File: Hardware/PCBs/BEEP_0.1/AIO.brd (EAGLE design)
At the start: 110 x 110 mm, 70 parts, among them IC1 ULN2803ASOP18, IC2 ULN2803ASOP18, IC3 74HC238D, IC4 74HC238D, U2 TB6612FNG, U3 ATXMEGA64D3-AU, X1 MICROMATCH-8, X10 MICROMATCH-10, X2 MICROMATCH-8, X3 MICROMATCH-8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

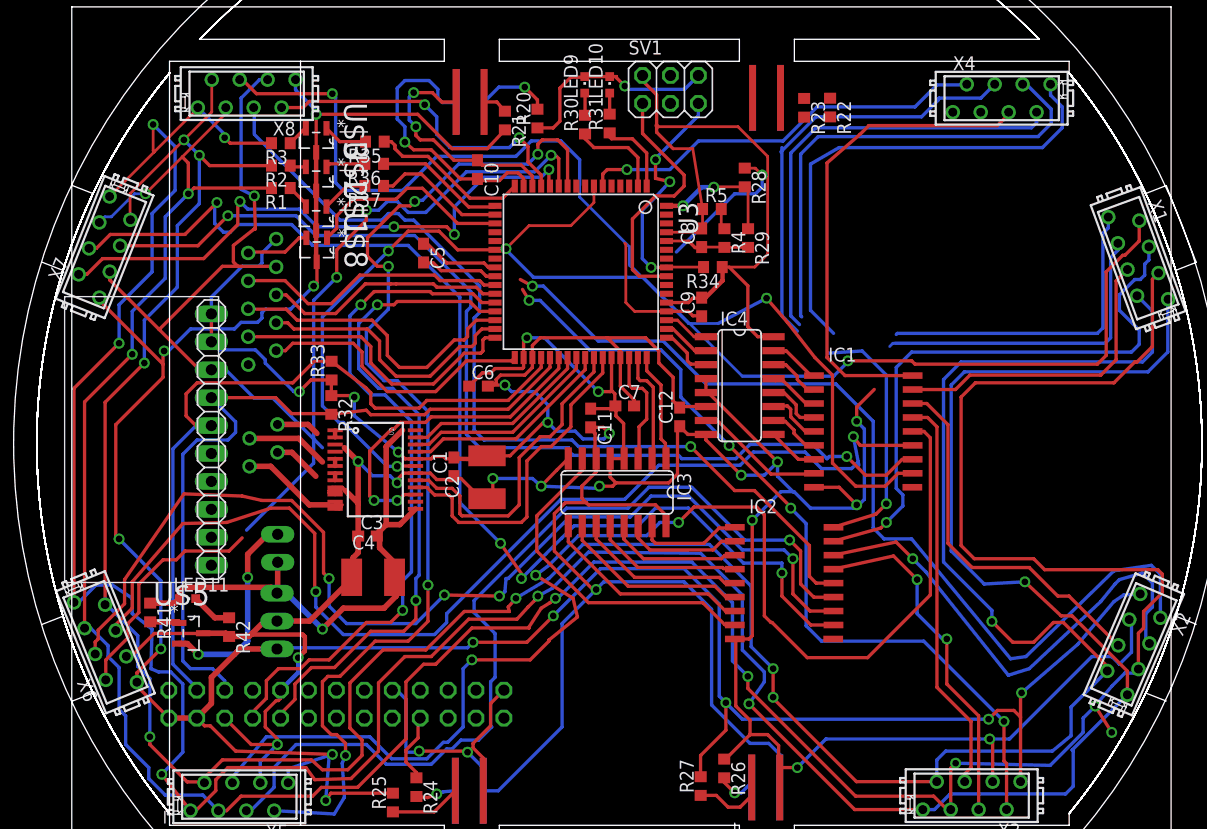
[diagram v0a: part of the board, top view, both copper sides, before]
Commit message: *add i2c connector *continue routing
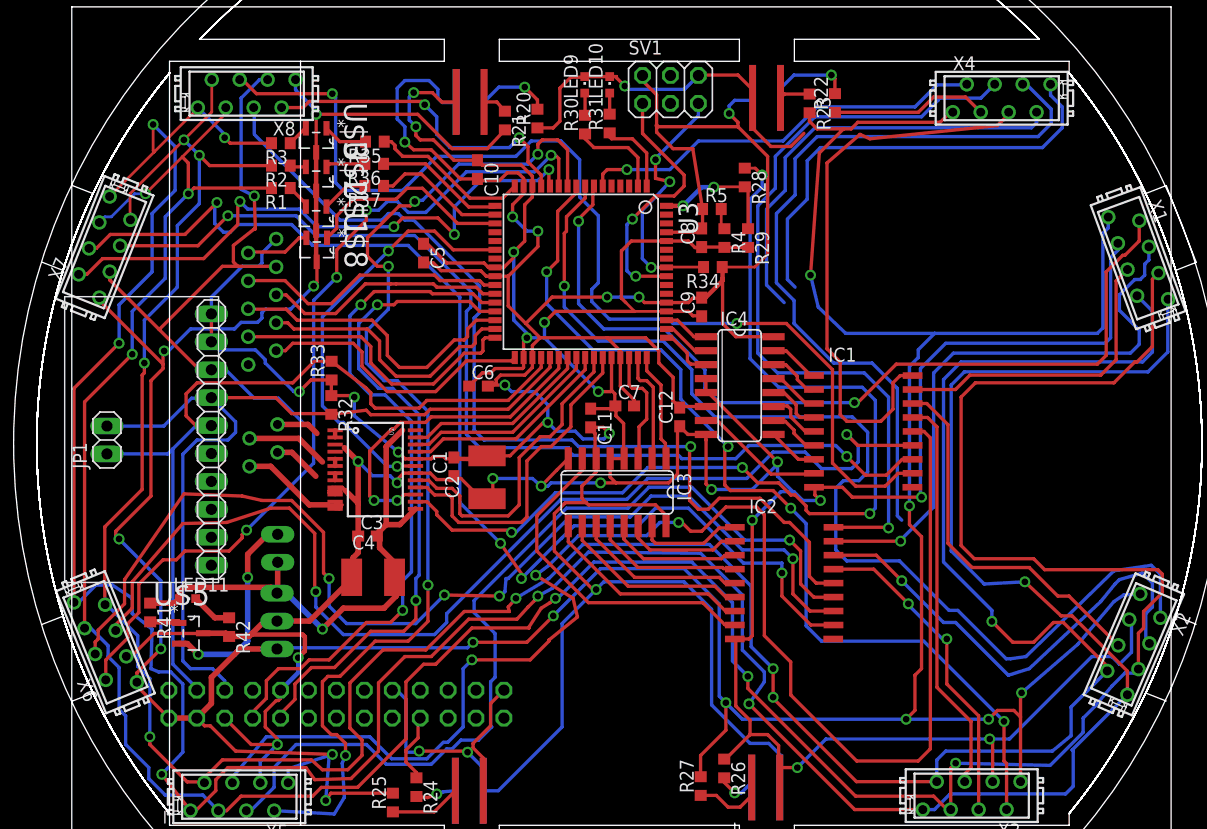
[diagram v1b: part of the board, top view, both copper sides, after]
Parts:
- added JP1: I2C, pinhead:1X02
- moved R23 0.64 mm to (67.1, 71.2)
- moved R22 0.61 mm to (69.4, 71.3), turned to 90 degrees
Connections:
- net SCL: now also JP1.2
- net SDA: now also JP1.1
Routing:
- net +5V: track 287.8 -> 364.9 mm, vias 12 -> 15
- net +7V: track 62.3 -> 138.7 mm, vias 3 -> 6
- net GND: track 451.0 -> 513.9 mm, vias 20 -> 22
- net +3V3: track 298.6 -> 336.9 mm, vias 10 -> 15
- net LED_A2_OUT: track 327.8 -> 351.2 mm, vias 8 -> 6
- net LED_K4_OUT: track 116.5 -> 136.0 mm
- net ADISTANCE_2: track 86.2 -> 99.3 mm
- net ADISTANCE_3: track 75.4 -> 86.8 mm
- net SCL: track 68.2 -> 78.8 mm
- net IR_LED_K0_OUT: track 62.6 -> 71.8 mm
- net ENCODER_L2: track 0.00 -> 7.81 mm, vias 0 -> 1
- net LED_K0_OUT: track 44.6 -> 51.6 mm
- net SDA: track 70.0 -> 76.2 mm
- net ADISTANCE_1: track 85.4 -> 79.4 mm
- net IR_LED_K7_OUT: track 82.6 -> 86.6 mm
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
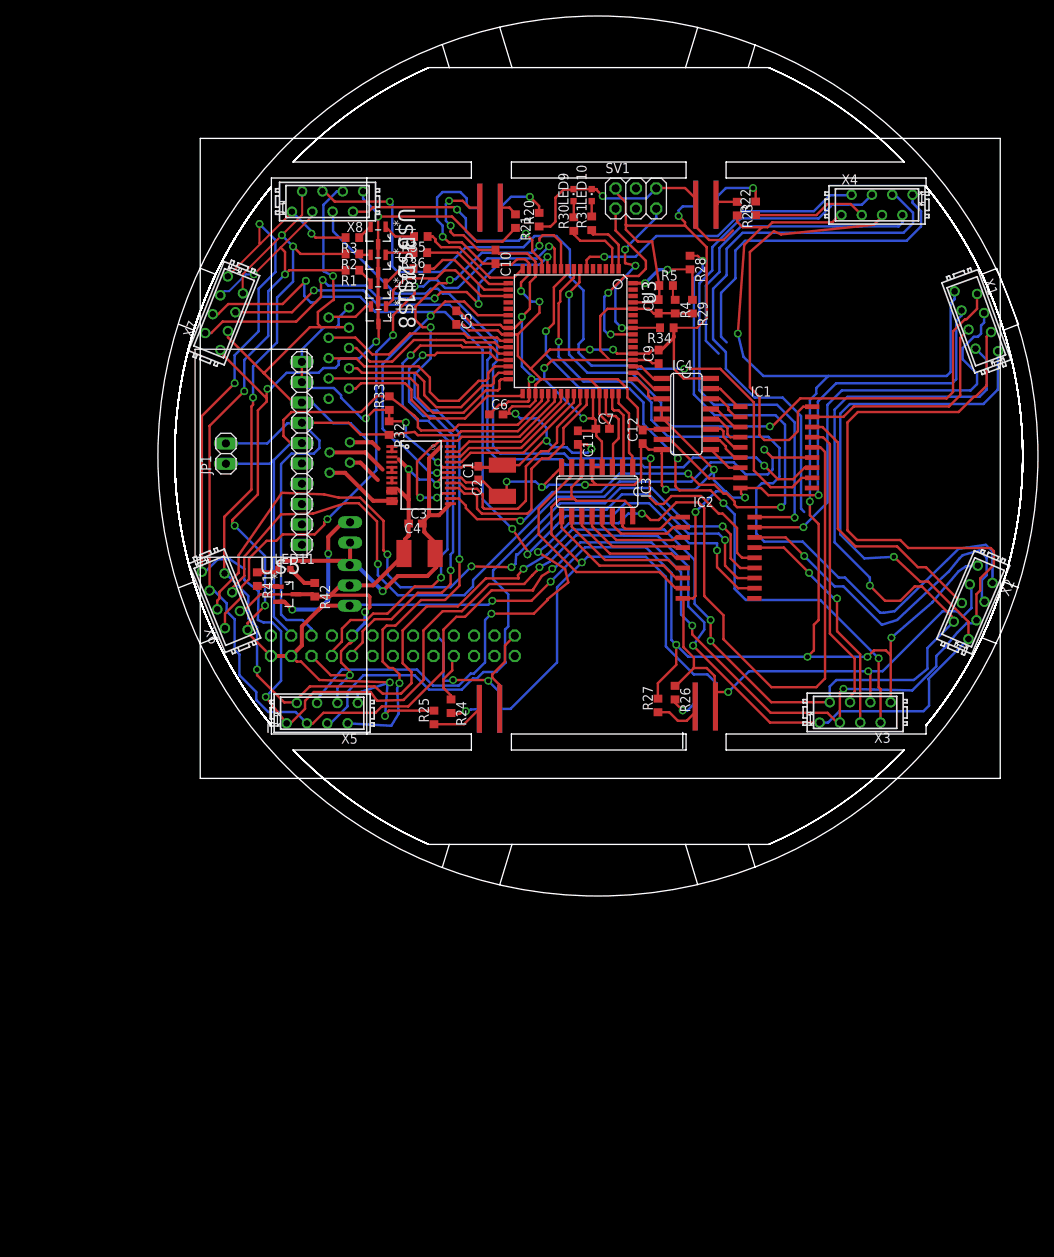
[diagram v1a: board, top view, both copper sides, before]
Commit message: add i2c header continue routing
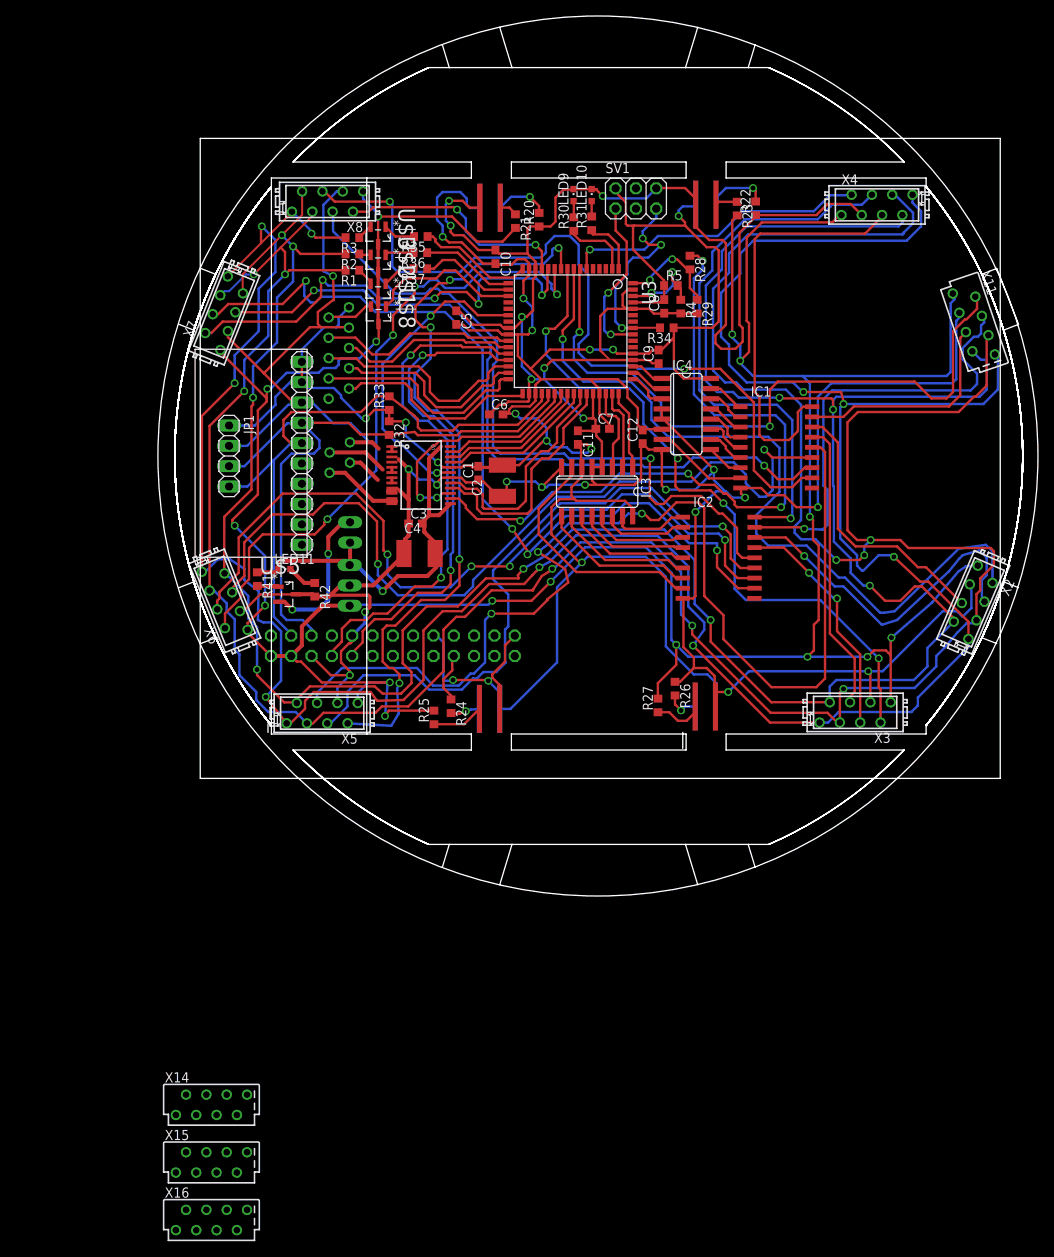
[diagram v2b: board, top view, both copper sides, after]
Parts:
- removed X1: MICROMATCH-8, Con-amp-micromatch:MICROMATCH-8
- added X11, X14, X15, X16: (no value), con-amp:FSIDE-8
- JP1: value I2C -> (none); device pinhead:1X02 -> pinhead:1X04
- moved C8 0.70 mm to (58.0, 59.0)
- moved R4 0.70 mm to (60.1, 59.0)
- moved R5 0.60 mm to (58.8, 61.6)
- moved R29 0.60 mm to (62.1, 59.0)
- moved JP1 0.50 mm to (3.60, 40.3), turned to 270 degrees
- moved R26 0.50 mm to (59.4, 11.2)
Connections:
- net +3V3: now also JP1.1
- net +5V: now also X11.1; no longer X1.8
- net ADISTANCE_1: now also X11.2; no longer X1.7
- net GND: now also JP1.2, X11.3; no longer X1.6
- net IR_LED_K1_OUT: now also X11.4; no longer X1.5
- net LED_A0_OUT: now also X11.8; no longer X1.1
- net LED_A1_OUT: now also X11.7; no longer X1.2
- net LED_A2_OUT: now also X11.6; no longer X1.3
- net LED_K1_OUT: now also X11.5; no longer X1.4
- net SCL: now also JP1.3; no longer JP1.2
- net SDA: now also JP1.4; no longer JP1.1
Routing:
- net GND: track 513.9 -> 567.9 mm
- net LED_A1_OUT: track 311.7 -> 333.7 mm, vias 8 -> 9
- net LED_A0_OUT: track 328.1 -> 349.1 mm, vias 7 -> 9
- net LED_A2_OUT: track 351.2 -> 367.4 mm, vias 6 -> 9
- net +5V: track 364.9 -> 380.9 mm, vias 15 -> 16
- net +3V3: track 336.9 -> 350.5 mm
- net N$4: track 2.08 -> 11.2 mm, vias 0 -> 2
- net LED_K5_OUT: track 99.9 -> 105.6 mm
- net ADISTANCE_1: track 79.4 -> 83.7 mm
- net PDI_DATA: track 23.7 -> 20.8 mm
- net IR_LED_K1_OUT: track 53.5 -> 56.1 mm
- net PDI_CLK: track 23.7 -> 26.1 mm
- net BATT_VOLTAGE: track 11.8 -> 14.1 mm
- net ADISTANCE_6: track 54.0 -> 56.4 mm
- net LED_K7_OUT: track 97.7 -> 99.8 mm
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
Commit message: continue routing add hardware architecture shematic
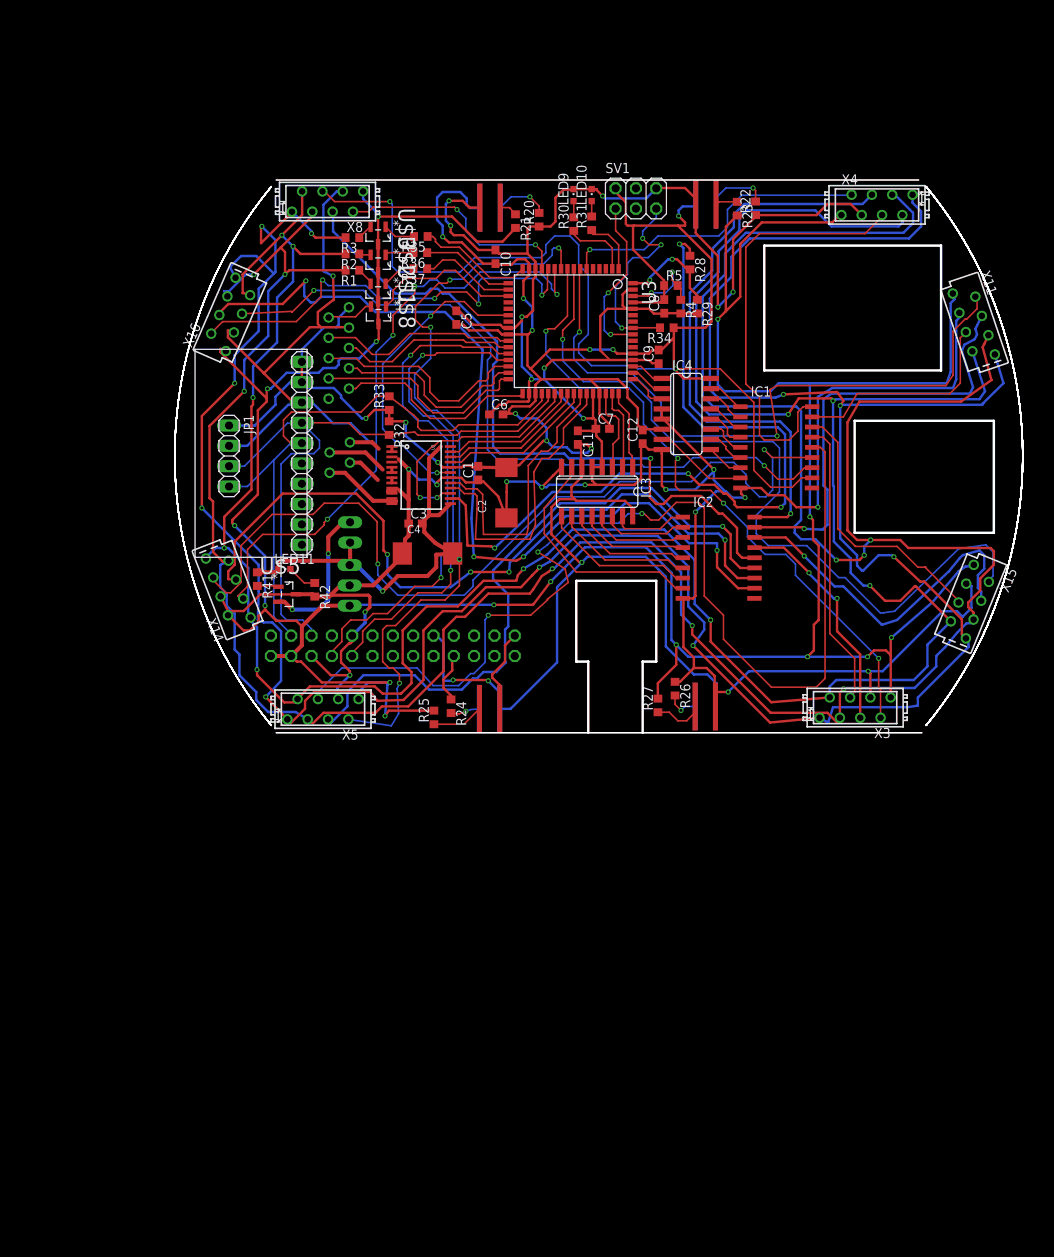
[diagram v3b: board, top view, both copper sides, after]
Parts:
- removed X2, X6, X7: MICROMATCH-8, Con-amp-micromatch:MICROMATCH-8
- C2, C4: device rcl:C1812 -> rcl:SMC_D
- moved X15 117.9 mm to (96.2, 22.1), turned to 247.9 degrees
- moved X16 113.2 mm to (3.80, 58.0), turned to 66.5 degrees
- moved X14 64.6 mm to (3.50, 23.8), turned to 111.2 degrees
- moved C2 1.58 mm to (38.3, 35.7)
- moved C4 1.00 mm to (28.4, 28.1)
- moved X3 0.60 mm to (81.9, 8.85)
- moved X5 0.51 mm to (15.3, 8.65)
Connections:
- net +3V3: now also C2.-; no longer C2.2
- net +5V: now also X14.2, X15.1, X16.1; no longer X2.8, X6.8, X7.8
- net +7V: now also C4.-; no longer C4.2
- net ADISTANCE_2: now also X15.2; no longer X2.7
- net ADISTANCE_5: now also X14.3; no longer X6.7
- net ADISTANCE_6: now also X16.2; no longer X7.7
- net GND: now also C2.+, C4.+, X14.4, X15.3, X16.3; no longer C2.1, C4.1, X2.6, X6.6, X7.6
- net IR_LED_K2_OUT: now also X15.4; no longer X2.5
- net IR_LED_K5_OUT: now also X14.5; no longer X6.5
- net IR_LED_K6_OUT: now also X16.4; no longer X7.5
- net LED_A0_OUT: now also X15.8, X16.8; no longer X2.1, X6.1, X7.1
- net LED_A1_OUT: now also X14.8, X15.7, X16.7; no longer X2.2, X6.2, X7.2
- net LED_A2_OUT: now also X14.7, X15.6, X16.6; no longer X2.3, X6.3, X7.3
- net LED_K2_OUT: now also X15.5; no longer X2.4
- net LED_K5_OUT: now also X14.6; no longer X6.4
- net LED_K6_OUT: now also X16.5; no longer X7.4
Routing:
- net +7V: track 138.7 -> 151.1 mm
- net LED_A1_OUT: track 333.7 -> 343.0 mm, vias 9 -> 10
- net MOTOR_B_IN1: track 28.9 -> 35.8 mm
- net MOTOR_B_IN2: track 30.5 -> 37.4 mm
- net LED_A2_OUT: track 367.4 -> 372.9 mm
- net IR_LED_K6_OUT: track 106.0 -> 111.1 mm
- net GND: track 567.9 -> 563.1 mm, vias 22 -> 24
- net ADISTANCE_3: track 87.2 -> 82.7 mm
- net ADISTANCE_5: track 80.6 -> 76.7 mm
- net +5V: track 380.9 -> 384.6 mm, vias 16 -> 15
- net LED_K5_OUT: track 105.6 -> 109.0 mm
- net LED_A0_OUT: track 349.1 -> 352.5 mm, vias 9 -> 10
- net IR_LED_K5_OUT: track 96.7 -> 93.5 mm
- net IR_LED_K0_OUT: track 71.0 -> 73.3 mm
- net +3V3: track 350.5 -> 348.5 mm
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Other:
- board size 110 x 110 mm -> 106 x 69.1 mm

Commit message: add momentary push button with mosfet latch circuit as on/off switch continue routing
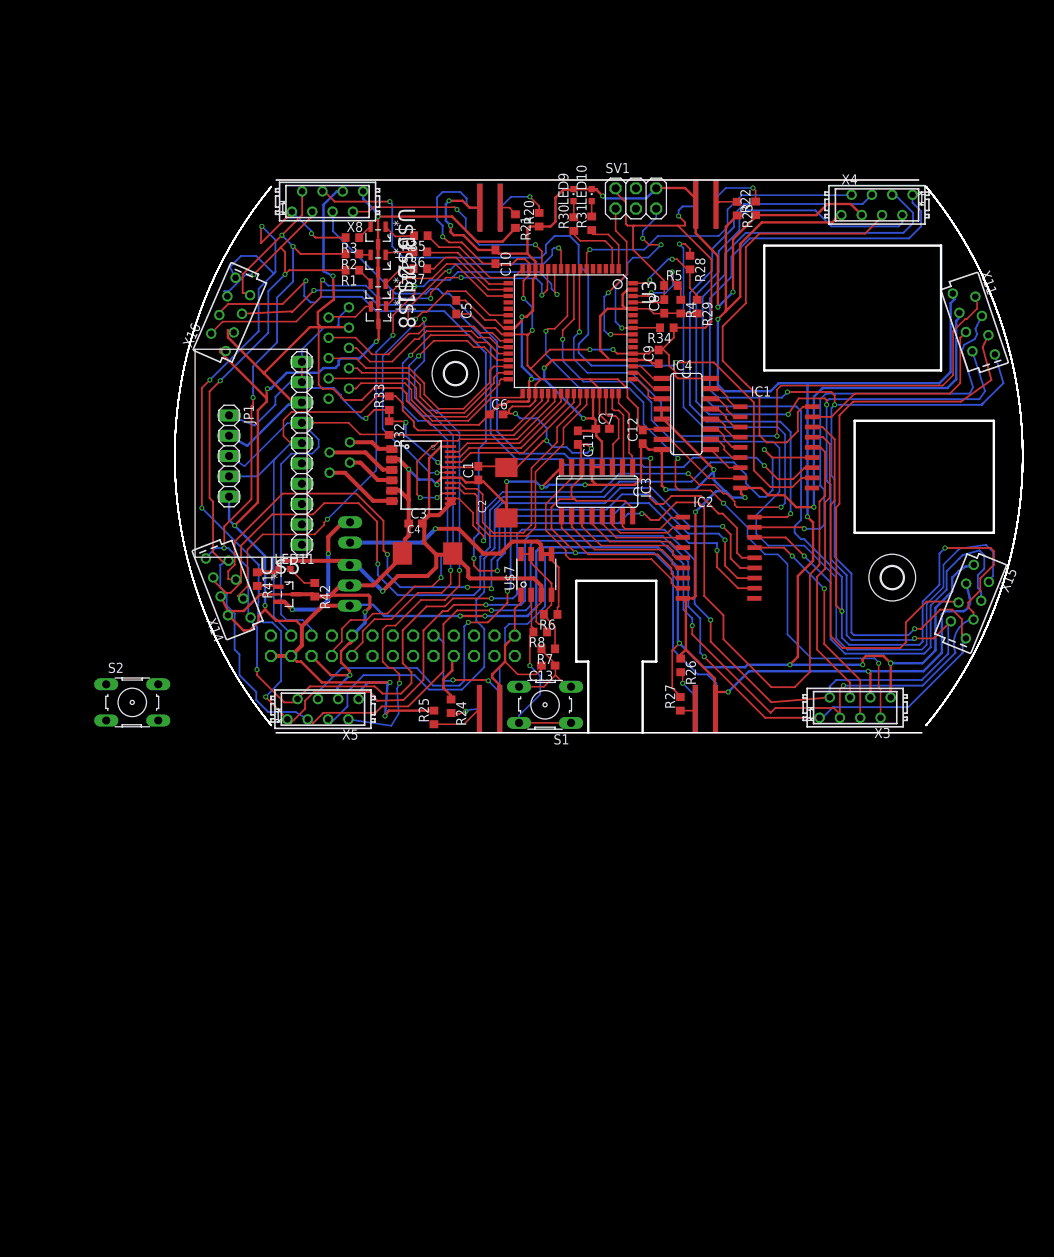
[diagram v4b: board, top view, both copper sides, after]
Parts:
- added C13: 1uF, rcl:C0603
- added R6, R8: 10k, rcl:R0603
- added R7: 100k, rcl:R0603
- added S1, S2: (no value), switch-omron:B3F-10XX
- added U$4, U$6: (no value), holes:2,8
- added U$7: DMC3028LSD, BEEP:SO08
- JP1: device pinhead:1X04 -> pinhead:1X05
- moved R26 2.98 mm to (60.0, 14.1)
- moved R27 2.81 mm to (60.0, 9.32)
- moved C5 1.30 mm to (32.0, 58.9)
- moved U$24 0.30 mm to (63.1, 11.7)
- moved R35 0.10 mm to (27.6, 67.8)
- moved R36 0.10 mm to (27.5, 65.8)
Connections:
- new net BATT_U: JP13.1, R6.1, U$7.5, U$7.6
- new net N$16: C13.1, R7.2, S1.3, S1.4
- new net N$18: R8.2, S1.1, S1.2, U$7.2
- new net N$22: R6.2, R7.1, U$7.4, U$7.7, U$7.8
- net +5V: now also JP1.5
- net +7V: now also R8.1, U$7.3; no longer JP13.1
- net GND: now also C13.2, U$7.1
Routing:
- net GND: track 563.1 -> 600.5 mm
- net BATT_U: track 0.00 -> 37.1 mm, vias 0 -> 1
- net LED_A2_OUT: track 372.9 -> 404.0 mm, vias 9 -> 8
- net N$18: track 0.00 -> 24.5 mm, vias 0 -> 1
- net +7V: track 151.1 -> 171.1 mm, vias 6 -> 5
- net N$22: track 0.00 -> 15.2 mm
- net LED_K2_OUT: track 34.0 -> 48.8 mm
- net +5V: track 384.6 -> 398.4 mm, vias 15 -> 16
- net ADISTANCE_2: track 98.1 -> 111.2 mm
- net N$16: track 0.00 -> 11.7 mm
- net IR_LED_K2_OUT: track 43.1 -> 54.8 mm
- net LED_A1_OUT: track 343.0 -> 354.0 mm
- net LED_A0_OUT: track 352.5 -> 361.2 mm
- net IR_LED_K6_OUT: track 111.1 -> 117.1 mm
- net MOTOR_A_OUT2: track 8.17 -> 13.8 mm
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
